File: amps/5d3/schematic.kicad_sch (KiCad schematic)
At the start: 43 parts, among them T2 PP : 8

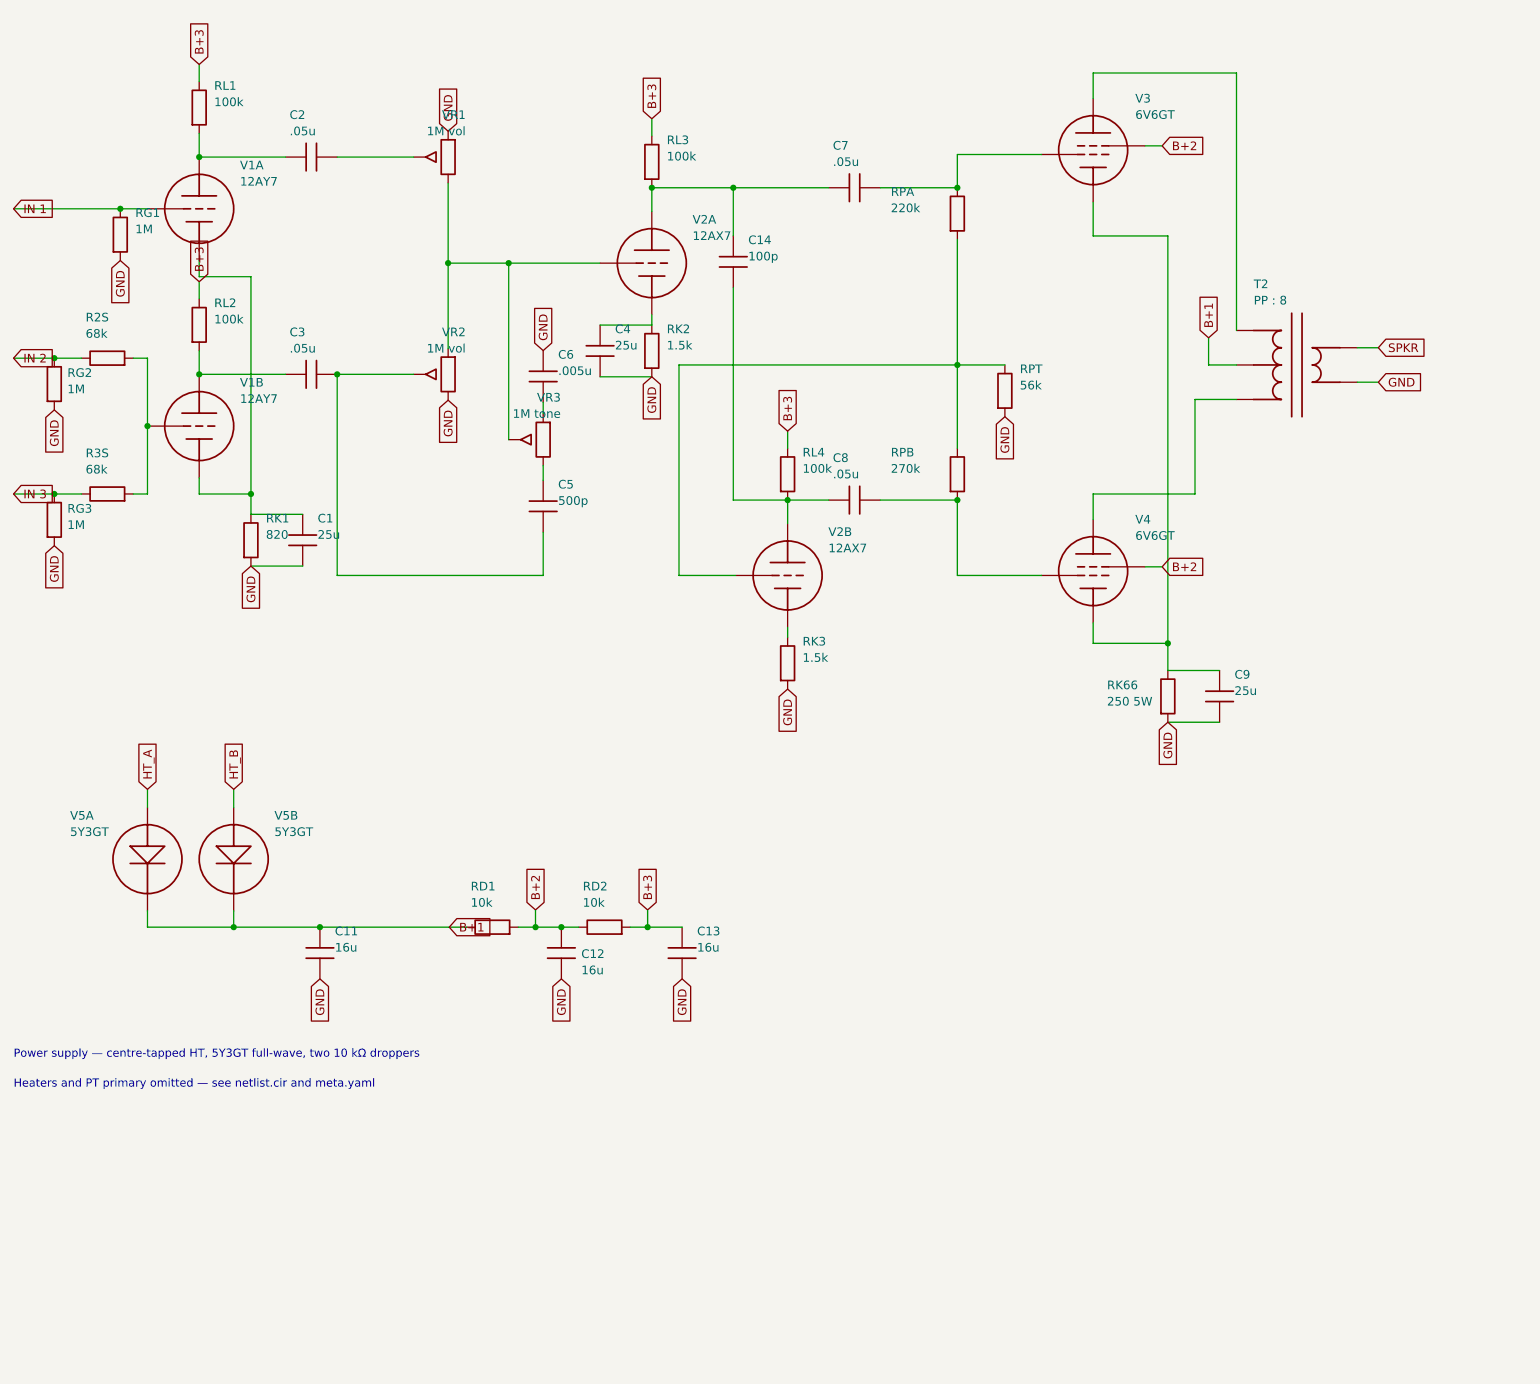
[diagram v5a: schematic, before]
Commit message: Add: real tube pin numbers and readable valve glyphs on every schematic
Phase B of the drawing program. A factory service sheet numbers every tube
pin, because the number is what a technician puts a probe on. This corpus
printed none, and the numbers hidden in its symbols were positional
placeholders (P=1, G=2, K=3) that would have published a 6V6GT's plate as
pin 1 when it is pin 3.

1055 electrodes now carry the real number, 1027 lettered (27 are shared
filaments deduped, 1 dropped for want of clear space on the 6G2). Resolved per
instance from reference/tubes/<slug>.yaml through the same alias resolution the
layout renderer uses, so a 12AX7 section and a 6SL7 section each get their own
basing. A valve whose basing the corpus does not carry prints nothing rather
than a wrong number.

Section letters and basing units are now separate things, which cost a detour
worth recording. The RCA 12AX7-A sheet reads "Pin 1 - Plate of Unit No.2 ...
Pin 6 - Plate of Unit No.1", so unit numbering is not pin order; the 5Y3 and
GZ34 number their units in opposite pin order, so nothing positional can
express it. But the section LETTER is a designator, not a basing fact: this
corpus, like every technician, calls the first stage in signal order V1A, and
five amps' prose already did. On four amps the factory sheets put that first
stage on the other half -- the AA764's own schematic prints +200 V on pin 1 --
so those drawings now state their unit explicitly, each citing its source, and
no letter, netlist, parts list or layout comment changed. 183 layout comments
agree with the printed numbers, 0 disagree. A guard fires if two halves of one
bottle resolve to the same unit, which is exactly how this was found.

Glyphs: the cathode gains a bracket and filament hairpin so it can no longer be
confused with the plate bar, the pentode's screen sits on its own row, and a
rectifier draws as one envelope over its sections instead of two apparent
bottles. Line weights are scaled per sheet to a co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
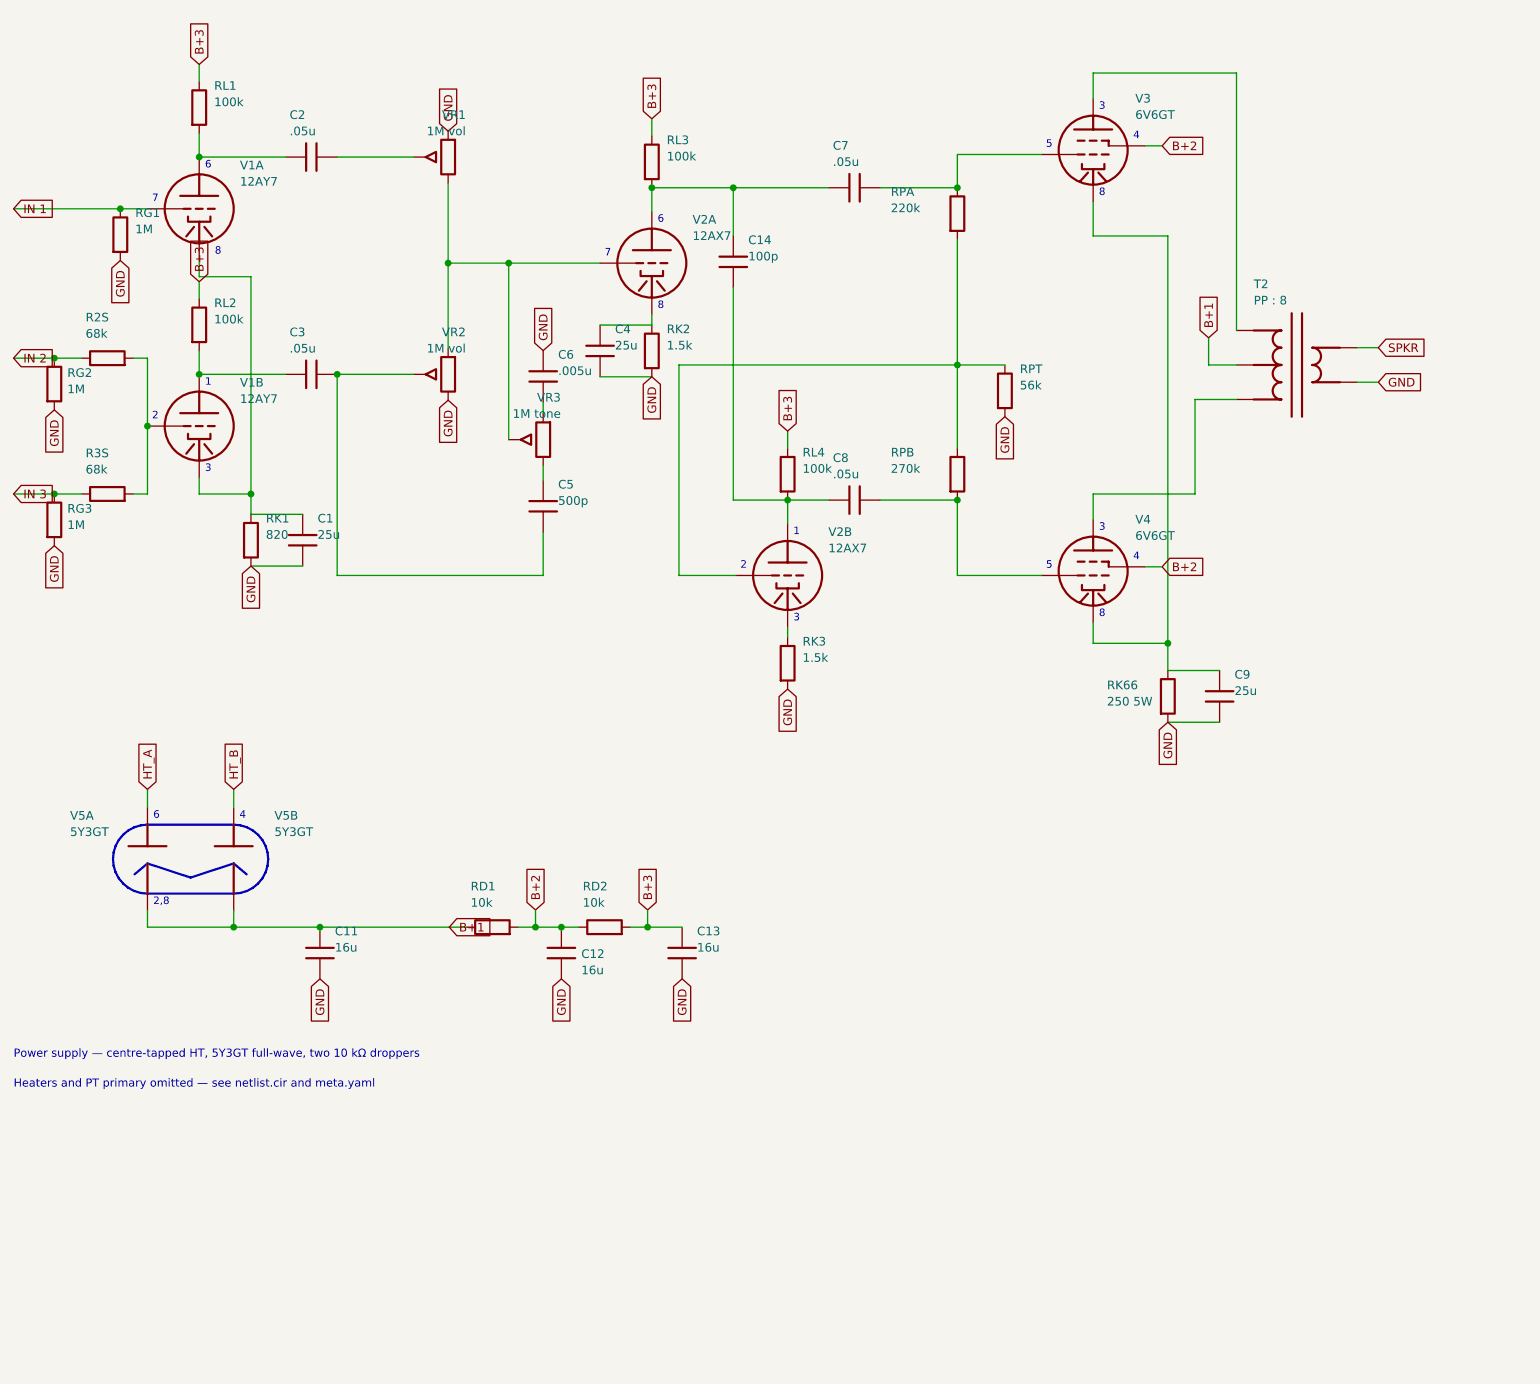
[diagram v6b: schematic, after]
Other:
- note added: "1"
- note added: "2"
- note added: "2,8"
- note added: "3"
- note added: "4"
- note added: "5"
- note added: "6"
- note added: "7"
- note added: "8"
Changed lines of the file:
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@@
   (wire (pts (xy 12.7 38.278) (xy 28.42 38.278))
     (stroke (width 0) (type default)))
-  (junction (at 28.42 38.278) (diameter 0) (color 0 0 0 0))
+  (junction (at 28.42 38.278) (diameter 1) (color 0 0 0 0))
   (symbol (lib_id "cx:R") (at 28.42 42.088 0) (unit 1)
     (in_bom yes) (on_board yes)
@@
   (wire (pts (xy 12.7 60.278) (xy 18.7 60.278))
     (stroke (width 0) (type default)))
-  (junction (at 18.7 60.278) (diameter 0) (color 0 0 0 0))
+  (junction (at 18.7 60.278) (diameter 1) (color 0 0 0 0))
   (symbol (lib_id "cx:R") (at 18.7 64.088 0) (unit 1)
     (in_bom yes) (on_board yes)
@@
   (wire (pts (xy 12.7 80.278) (xy 18.7 80.278))
     (stroke (width 0) (type default)))
-  (junction (at 18.7 80.278) (diameter 0) (color 0 0 0 0))
+  (junction (at 18.7 80.278) (diameter 1) (color 0 0 0 0))
   (symbol (lib_id "cx:R") (at 18.7 84.088 0) (unit 1)
     (in_bom yes) (on_board yes)
@@
   (wire (pts (xy 32.42 70.278) (xy 32.42 80.278))
     (stroke (width 0) (type default)))
-  (junction (at 32.42 70.278) (diameter 0) (color 0 0 0 0))
+  (junction (at 32.42 70.278) (diameter 1) (color 0 0 0 0))
   (symbol (lib_id "cx:TRIODE") (at 40.04 70.278 0) (unit 1)
     (in_bom yes) (on_board yes)
@@
   (wire (pts (xy 47.66 80.278) (xy 47.66 83.278))
     (stroke (width 0) (type default)))
-  (junction (at 47.66 80.278) (diameter 0) (color 0 0 0 0))
+  (junction (at 47.66 80.278) (diameter 1) (color 0 0 0 0))
   (symbol (lib_id "cx:R") (at 47.66 87.088 0) (unit 1)
     (in_bom yes) (on_board yes)
@@
   (wire (pts (xy 40.04 30.658) (xy 52.74 30.658))
     (stroke (width 0) (type default)))
-  (junction (at 40.04 30.658) (diameter 0) (color 0 0 0 0))
+  (junction (at 40.04 30.658) (diameter 1) (color 0 0 0 0))
   (symbol (lib_id "cx:C") (at 56.55 30.658 90) (unit 1)
     (in_bom yes) (on_board yes)
@@
   (wire (pts (xy 40.04 62.658) (xy 52.74 62.658))
     (stroke (width 0) (type default)))
-  (junction (at 40.04 62.658) (diameter 0) (color 0 0 0 0))
+  (junction (at 40.04 62.658) (diameter 1) (color 0 0 0 0))
   (symbol (lib_id "cx:C") (at 56.55 62.658 90) (unit 1)
     (in_bom yes) (on_board yes)
@@
   (wire (pts (xy 76.7 58.848) (xy 76.7 46.278))
     (stroke (width 0) (type default)))
-  (junction (at 76.7 46.278) (diameter 0) (color 0 0 0 0))
+  (junction (at 76.7 46.278) (diameter 1) (color 0 0 0 0))
   (symbol (lib_id "cx:POT") (at 90.7 72.278 180) (unit 1)
     (in_bom yes) (on_board yes)
@@
   (wire (pts (xy 85.62 72.278) (xy 85.62 46.278))
     (stroke (width 0) (type default)))
-  (junction (at 85.62 46.278) (diameter 0) (color 0 0 0 0))
+  (junction (at 85.62 46.278) (diameter 1) (color 0 0 0 0))
   (wire (pts (xy 90.7 68.468) (xy 90.7 66.778))
     (stroke (width 0) (type default)))
@@
   (wire (pts (xy 60.36 92.278) (xy 60.36 62.658))
     (stroke (width 0) (type default)))
-  (junction (at 60.36 62.658) (diameter 0) (color 0 0 0 0))
+  (junction (at 60.36 62.658) (diameter 1) (color 0 0 0 0))
   (symbol (lib_id "cx:TRIODE") (at 106.7 46.278 0) (unit 1)
     (in_bom yes) (on_board yes)
@@
   (global_label "GND" (shape input) (at 126.7 109.018 270)
     (effects (font (size 1.27 1.27)) (justify right)))
-  (junction (at 106.7 35.178) (diameter 0) (color 0 0 0 0))
+  (junction (at 106.7 35.178) (diameter 1) (color 0 0 0 0))
   (wire (pts (xy 106.7 35.178) (xy 118.7 35.178))
     (stroke (width 0) (type default)))
   (wire (pts (xy 118.7 35.178) (xy 132.75 35.178))
     (stroke (width 0) (type default)))
-  (junction (at 118.7 35.178) (diameter 0) (color 0 0 0 0))
+  (junction (at 118.7 35.178) (diameter 1) (color 0 0 0 0))
   (wire (pts (xy 118.7 35.178) (xy 118.7 42.278))
     (stroke (width 0) (type default)))
@@
   (wire (pts (xy 126.7 81.178) (xy 132.75 81.178))
     (stroke (width 0) (type default)))
-  (junction (at 126.7 81.178) (diameter 0) (color 0 0 0 0))
+  (junction (at 126.7 81.178) (diameter 1) (color 0 0 0 0))
   (symbol (lib_id "cx:C") (at 136.56 35.178 90) (unit 1)
     (in_bom yes) (on_board yes)
@@
   (wire (pts (xy 140.37 35.178) (xy 151.7 35.178))
     (stroke (width 0) (type default)))
-  (junction (at 151.7 35.178) (diameter 0) (color 0 0 0 0))
+  (junction (at 151.7 35.178) (diameter 1) (color 0 0 0 0))
   (wire (pts (xy 151.7 35.178) (xy 151.7 30.278))
     (stroke (width 0) (type default)))
@@
   (wire (pts (xy 140.37 81.178) (xy 151.7 81.178))
     (stroke (width 0) (type default)))
-  (junction (at 151.7 81.178) (diameter 0) (color 0 0 0 0))
+  (junction (at 151.7 81.178) (diameter 1) (color 0 0 0 0))
   (wire (pts (xy 151.7 81.178) (xy 151.7 92.278))
     (stroke (width 0) (type default)))
@@
   (wire (pts (xy 151.7 73.558) (xy 151.7 61.278))
     (stroke (width 0) (type default)))
-  (junction (at 151.7 61.278) (diameter 0) (color 0 0 0 0))
+  (junction (at 151.7 61.278) (diameter 1) (color 0 0 0 0))
   (wire (pts (xy 151.7 61.278) (xy 158.7 61.278))
     (stroke (width 0) (type default)))
@@
   (wire (pts (xy 182.7 102.278) (xy 182.7 106.278))
     (stroke (width 0) (type default)))
-  (junction (at 182.7 102.278) (diameter 0) (color 0 0 0 0))
+  (junction (at 182.7 102.278) (diameter 1) (color 0 0 0 0))
   (symbol (lib_id "cx:R") (at 182.7 110.088 0) (unit 1)
     (in_bom yes) (on_board yes)
@@
   (wire (pts (xy 57.82 144.078) (xy 76.87 144.078))
     (stroke (width 0) (type default)))
-  (junction (at 45.12 144.078) (diameter 0) (color 0 0 0 0))
-  (junction (at 57.82 144.078) (diameter 0) (color 0 0 0 0))
+  (junction (at 45.12 144.078) (diameter 1) (color 0 0 0 0))
+  (junction (at 57.82 144.078) (diameter 1) (color 0 0 0 0))
   (symbol (lib_id "cx:C") (at 57.82 147.888 0) (unit 1)
     (in_bom yes) (on_board yes)
@@
   (wire (pts (xy 93.38 144.078) (xy 95.92 144.078))
     (stroke (width 0) (type default)))
-  (junction (at 89.57 144.078) (diameter 0) (color 0 0 0 0))
+  (junction (at 89.57 144.078) (diameter 1) (color 0 0 0 0))
   (global_label "B+2" (shape input) (at 89.57 141.538 90)
     (effects (font (size 1.27 1.27)) (justify left)))
   (wire (pts (xy 89.57 141.538) (xy 89.57 144.078))
     (stroke (width 0) (type default)))
-  (junction (at 93.38 144.078) (diameter 0) (color 0 0 0 0))
+  (junction (at 93.38 144.078) (diameter 1) (color 0 0 0 0))
   (symbol (lib_id "cx:C") (at 93.38 147.888 0) (unit 1)
     (in_bom yes) (on_board yes)
@@
   (wire (pts (xy 106.08 144.078) (xy 111.16 144.078))
     (stroke (width 0) (type default)))
-  (junction (at 106.08 144.078) (diameter 0) (color 0 0 0 0))
+  (junction (at 106.08 144.078) (diameter 1) (color 0 0 0 0))
   (global_label "B+3" (shape input) (at 106.08 141.538 90)
     (effects (font (size 1.27 1.27)) (justify left)))
@@
   (global_label "GND" (shape input) (at 111.16 151.698 270)
     (effects (font (size 1.27 1.27)) (justify right)))
+  (polyline (pts (xy 45.12 128.978) (xy 46.111 129.076) (xy 47.064 129.365) (xy 47.942 129.834) (xy 48.712 130.466) (xy 49.344 131.236) (xy 49.813 132.114) (xy 50.102 133.067) (xy 50.2 134.058) (xy 50.102 135.049) (xy 49.813 136.002) (xy 49.344 136.88) (xy 48.712 137.65) (xy 47.942 138.282) (xy 47.064 138.751) (xy 46.111 139.04) (xy 45.12 139.138) (xy 32.42 139.138) (xy 31.429 139.04) (xy 30.476 138.751) (xy 29.598 138.282) (xy 28.828 137.65) (xy 28.196 136.88) (xy 27.727 136.002) (xy 27.438 135.049) (xy 27.34 134.058) (xy 27.438 133.067) (xy 27.727 132.114) (xy 28.196 131.236) (xy 28.828 130.466) (xy 29.598 129.834) (xy 30.476 129.365) (xy 31.429 129.076) (xy 32.42 128.978) (xy 45.12 128.978))
+    (stroke (width 0.324) (type default) (color 197 163 255 1)) (fill (type none)))
+  (polyline (pts (xy 30.52 136.293) (xy 32.42 134.693) (xy 38.77 136.773) (xy 45.12 134.693) (xy 47.02 136.293))
+    (stroke (width 0.324) (type default) (color 197 163 255 1)) (fill (type none)))
+  (text "6" (at 40.89 31.928 0)
+    (effects (font (size 1.1 1.1)) (justify left)))
+  (text "7" (at 33.0928 36.878 0)
+    (effects (font (size 1.1 1.1)) (justify left)))
+  (text "8" (at 42.34 44.628 0)
+    (effects (font (size 1.1 1.1)) (justify left)))
+  (text "1" (at 40.89 63.928 0)
+    (effects (font (size 1.1 1.1)) (justify left)))
+  (text "2" (at 33.0928 68.878 0)
+    (effects (font (size 1.1 1.1)) (justify left)))
+  (text "3" (at 40.89 76.628 0)
+    (effects (font (size 1.1 1.1)) (justify left)))
+  (text "6" (at 107.55 39.928 0)
+    (effects (font (size 1.1 1.1)) (justify left)))
+  (text "7" (at 99.7528 44.878 0)
+    (effects (font (size 1.1 1.1)) (justify left)))
+  (text "8" (at 107.55 52.628 0)
+    (effects (font (size 1.1 1.1)) (justify left)))
+  (text "1" (at 127.55 85.928 0)
+    (effects (font (size 1.1 1.1)) (justify left)))
+  (text "2" (at 119.753 90.878 0)
+    (effects (font (size 1.1 1.1)) (justify left)))
+  (text "3" (at 127.55 98.628 0)
+    (effects (font (size 1.1 1.1)) (justify left)))
+  (text "3" (at 172.55 23.293 0)
+    (effects (font (size 1.1 1.1)) (justify left)))
+  (text "5" (at 164.753 28.878 0)
+    (effects (font (size 1.1 1.1)) (justify left)))
+  (text "4" (at 177.6 27.608 0)
+    (effects (font (size 1.1 1.1)) (justify left)))
+  (text "8" (at 172.55 35.993 0)
+    (effects (font (size 1.1 1.1)) (justify left)))
+  (text "3" (at 172.55 85.293 0)
+    (effects (font (size 1.1 1.1)) (justify left)))
+  (text "5" (at 164.753 90.878 0)
+    (effects (font (size 1.1 1.1)) (justify left)))
+  (text "4" (at 177.6 89.608 0)
+    (effects (font (size 1.1 1.1)) (justify left)))
+  (text "8" (at 172.55 97.993 0)
+    (effects (font (size 1.1 1.1)) (justify left)))
+  (text "6" (at 33.27 127.708 0)
+    (effects (font (size 1.1 1.1)) (justify left)))
+  (text "2,8" (at 33.27 140.408 0)
+    (effects (font (size 1.1 1.1)) (justify left)))
+  (text "4" (at 45.97 127.708 0)
+    (effects (font (size 1.1 1.1)) (justify left)))
   (text "Power supply — centre-tapped HT, 5Y3GT full-wave, two 10 kΩ droppers" (at 12.7 162.856 0)
     (effects (font (size 1.2 1.2)) (justify left)))
